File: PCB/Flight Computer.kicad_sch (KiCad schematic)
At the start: 0 parts

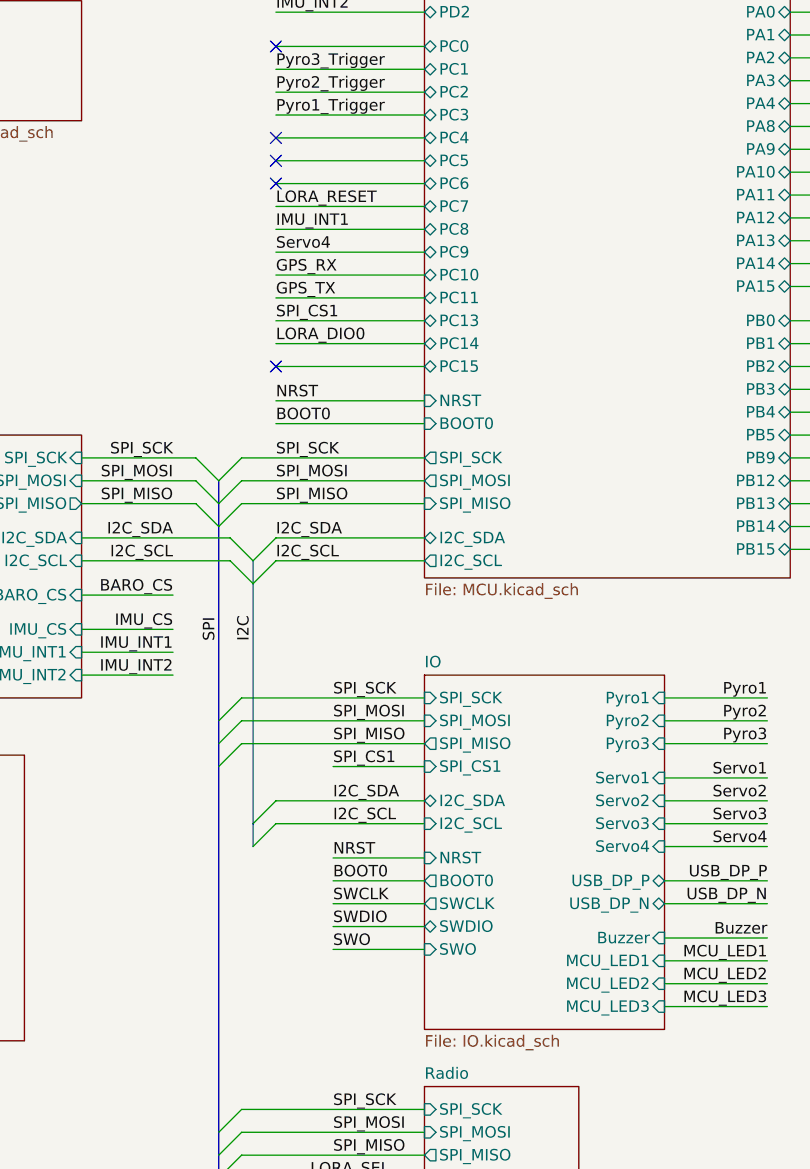
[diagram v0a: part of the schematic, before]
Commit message: Moved compass away from power traces, minor routing changes
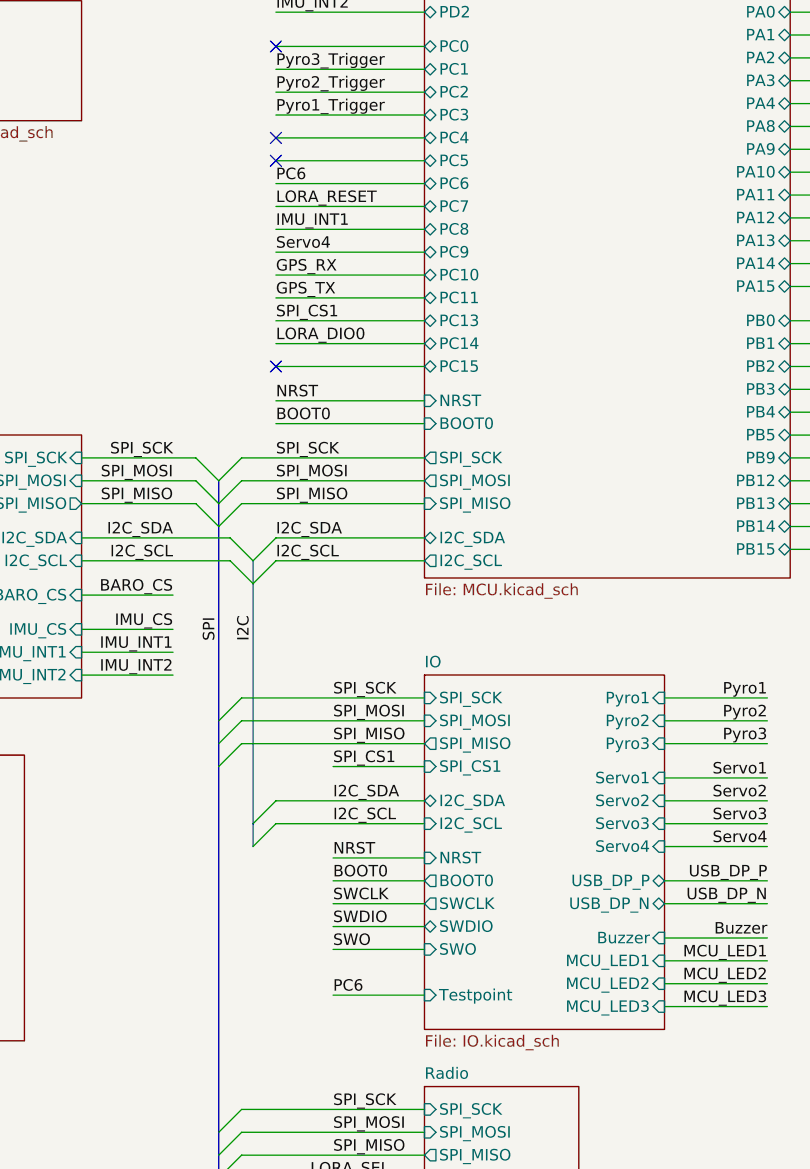
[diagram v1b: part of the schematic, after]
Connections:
- no-connect marks 15 -> 14
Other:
- sheet IO ports: added Testpoint; removed none
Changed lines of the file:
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@@
 		(at 104.14 175.26)
-	)
-	(no_connect
-		(at 100.33 50.8)
 	)
 	(bus_entry
@@
 	(wire
 		(pts
+			(xy 106.68 140.97) (xy 116.84 140.97)
+		)
+		(stroke
+			(width 0)
+			(type default)
+		)
+	)
+	(wire
+		(pts
 			(xy 157.48 81.28) (xy 173.99 81.28)
 		)
@@
 		)
 	)
+	(label "PC6"
+		(at 106.68 140.97 0)
+		(effects
+			(font
+				(size 1.27 1.27)
+			)
+			(justify left bottom)
+		)
+	)
 	(label "Pyro1_Cont"
 		(at 173.99 34.29 180)
@@
 	(label "I2C_SDA"
 		(at 106.68 119.38 0)
+		(effects
+			(font
+				(size 1.27 1.27)
+			)
+			(justify left bottom)
+		)
+	)
+	(label "PC6"
+		(at 100.33 50.8 0)
 		(effects
 			(font
@@
 			)
 		)
+		(pin "Testpoint" input
+			(at 116.84 140.97 180)
+			(effects
+				(font
+					(size 1.27 1.27)
+				)
+				(justify left)
+			)
+		)

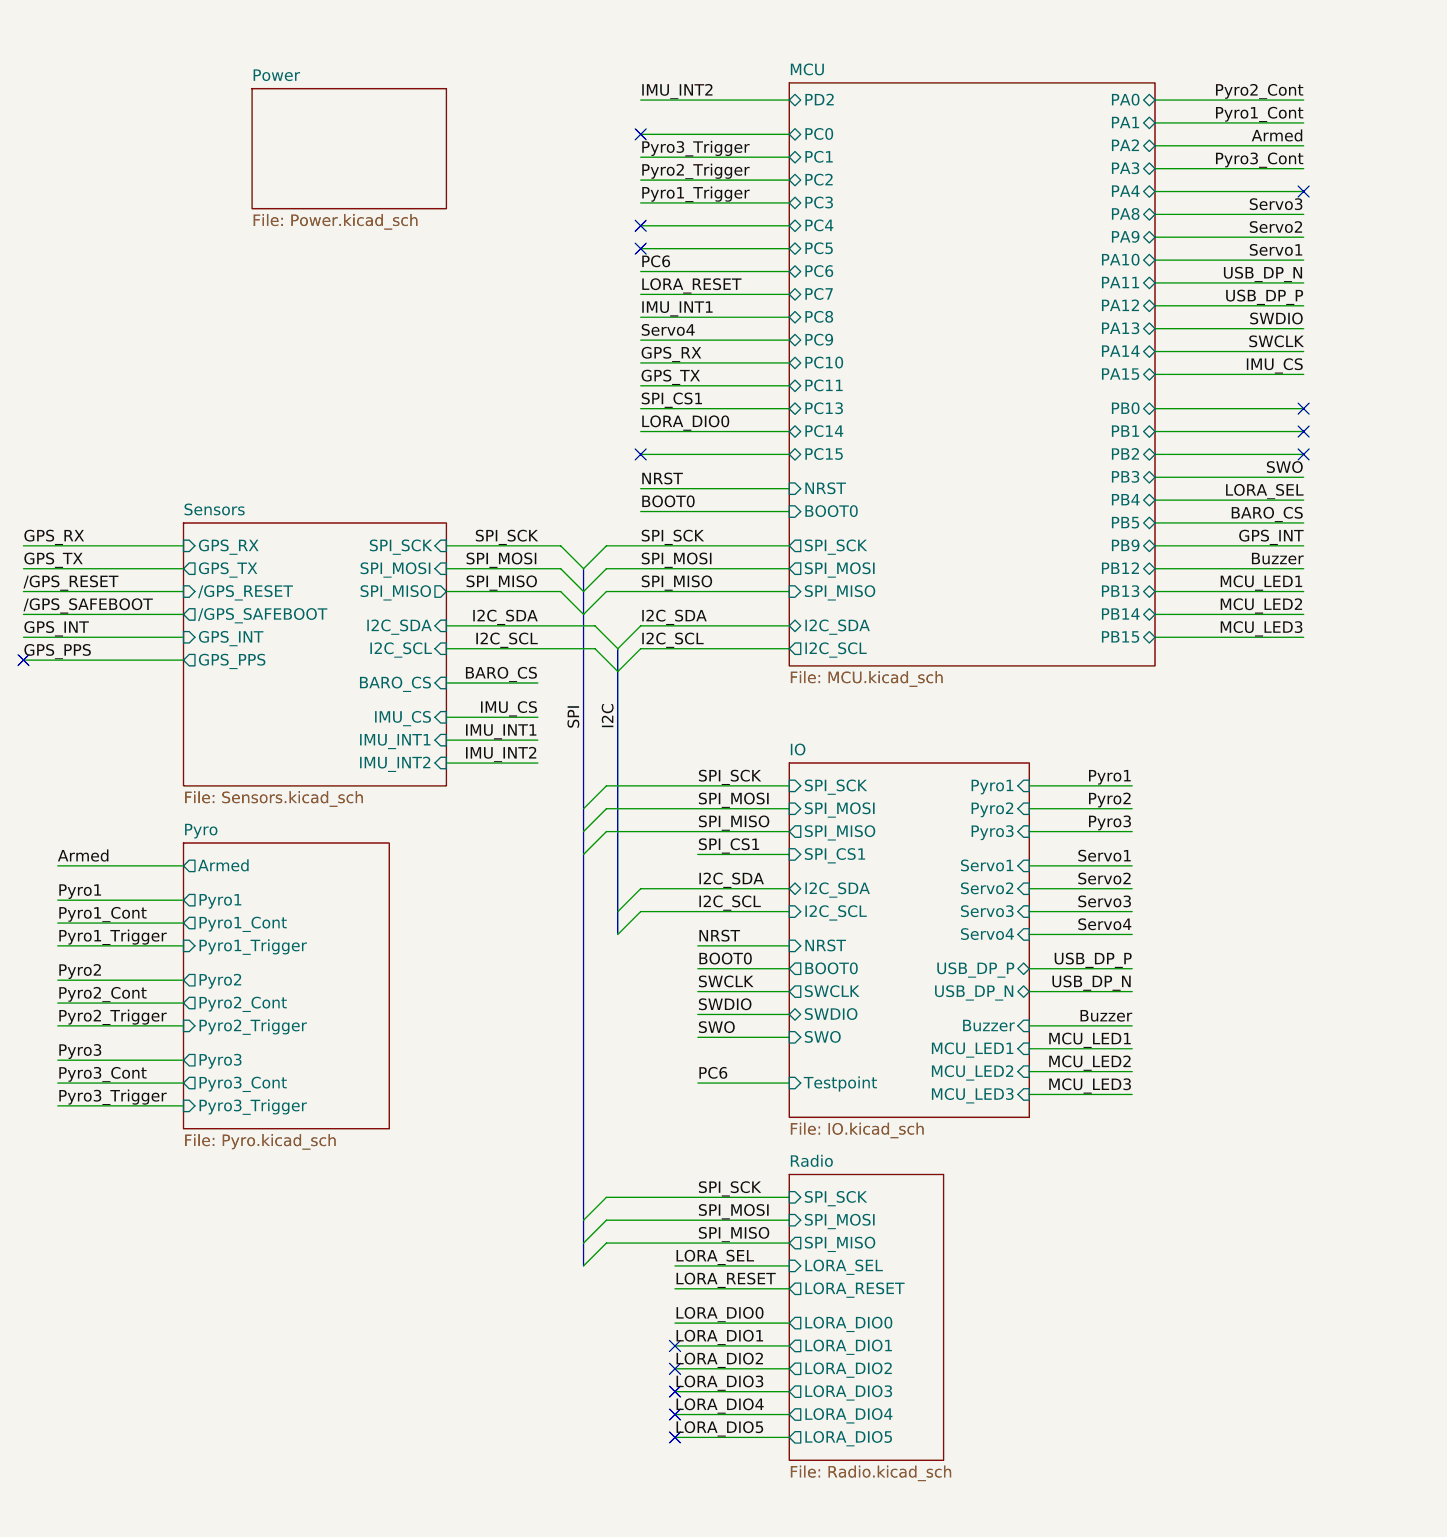
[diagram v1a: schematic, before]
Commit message: Added two more GPIO test pads
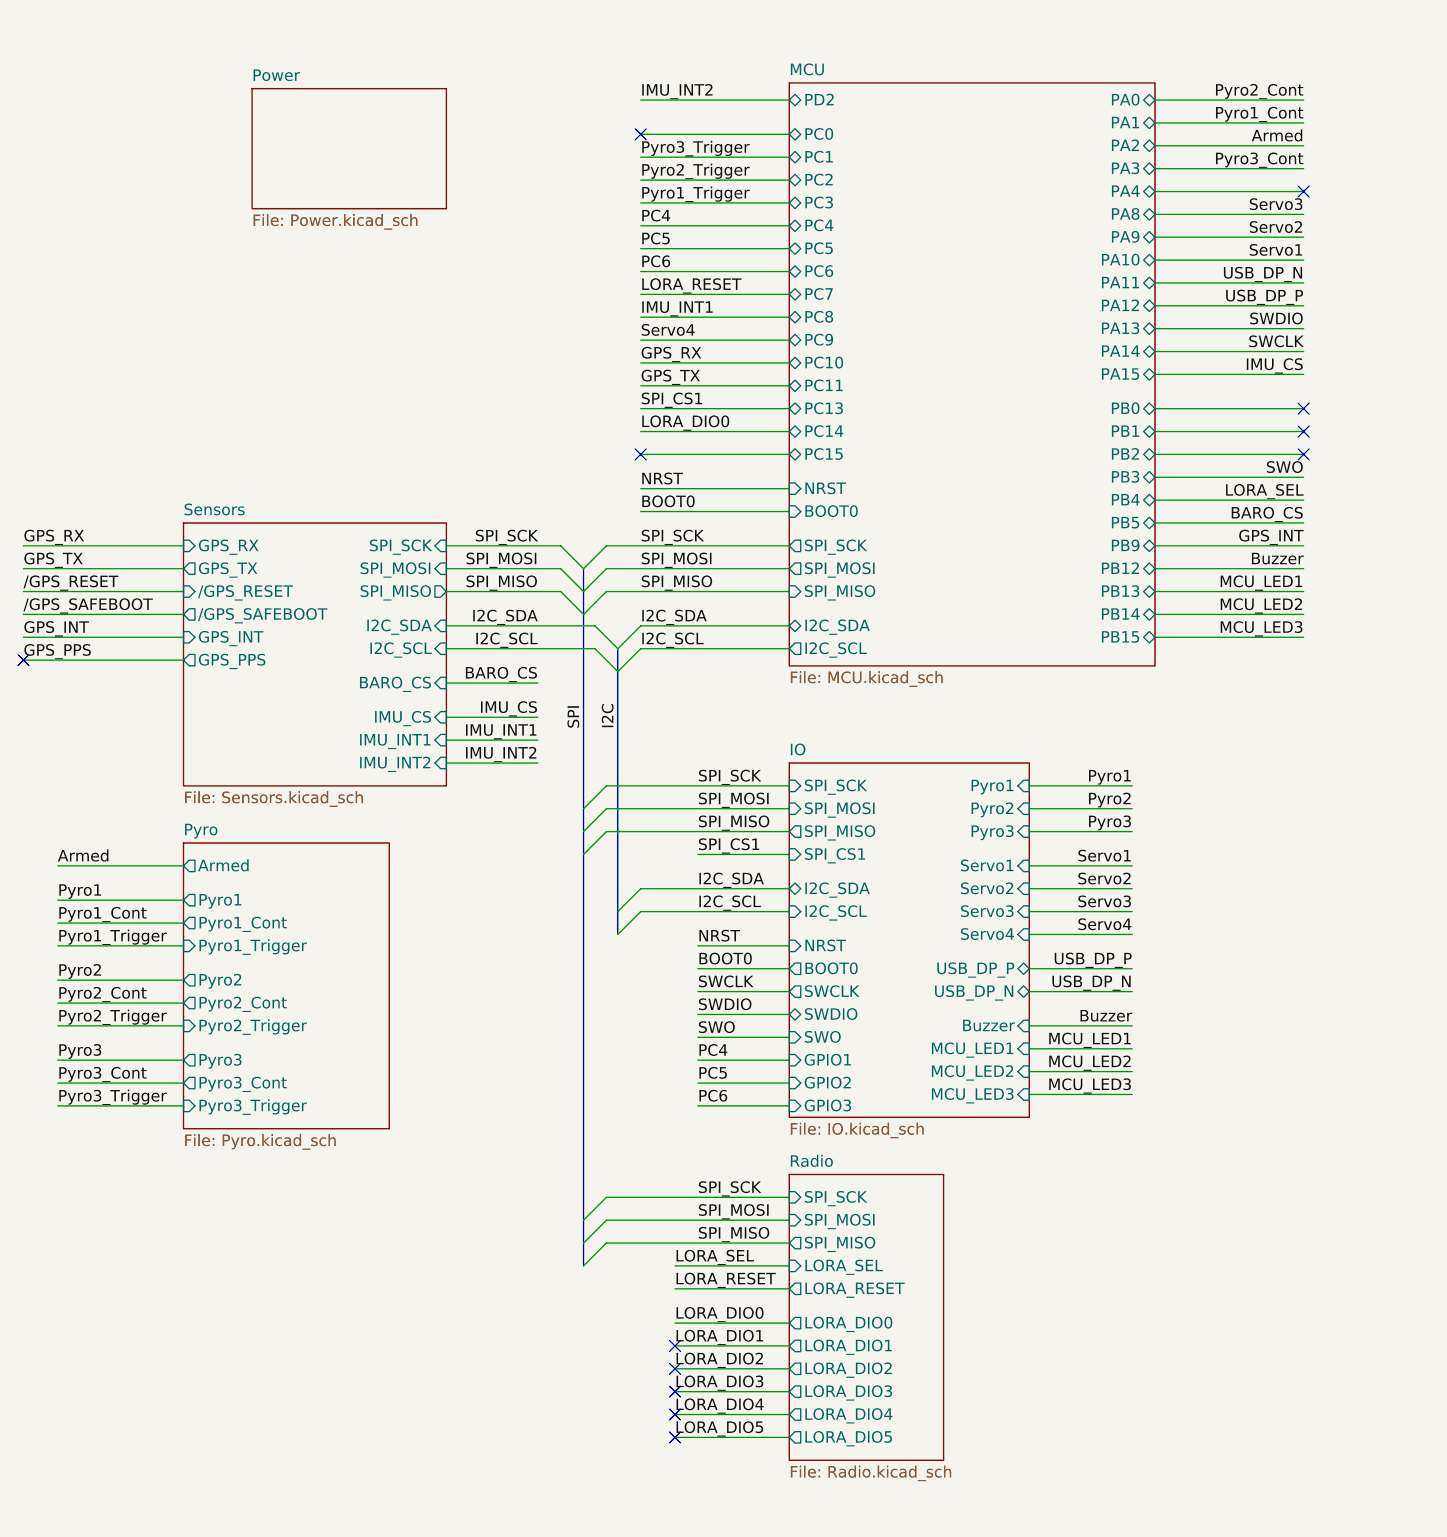
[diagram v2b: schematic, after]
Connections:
- no-connect marks 14 -> 12
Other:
- sheet IO ports: added GPIO1, GPIO2, GPIO3; removed Testpoint

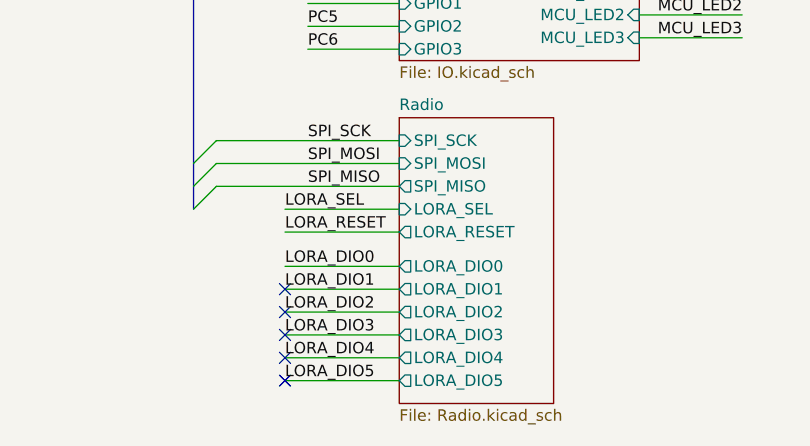
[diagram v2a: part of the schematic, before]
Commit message: Replaced the radio in the schematic
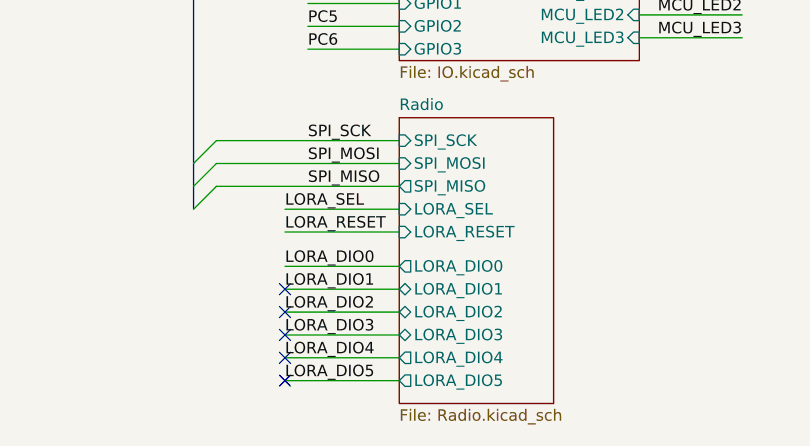
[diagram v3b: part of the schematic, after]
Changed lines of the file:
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@@
 (kicad_sch
-	(version 20250114)
+	(version 20260306)
 	(generator "eeschema")
-	(generator_version "9.0")
+	(generator_version "10.0")
 	(paper "A4")
 	(title_block
@@
 		)
 		(fill
-			(color 0 0 0 0.0000)
+			(color 0 0 0 0)
 		)
 		(property "Sheetname" "IO"
 			(at 116.84 104.6984 0)
+			(show_name no)
+			(do_not_autoplace no)
 			(effects
 				(font
@@
 		(property "Sheetfile" "IO.kicad_sch"
 			(at 116.84 145.3646 0)
+			(show_name no)
+			(do_not_autoplace no)
 			(effects
 				(font
@@
 		)
 		(fill
-			(color 0 0 0 0.0000)
+			(color 0 0 0 0)
 		)
 		(property "Sheetname" "Radio"
 			(at 116.84 150.4184 0)
+			(show_name no)
+			(do_not_autoplace no)
 			(effects
 				(font
@@
 		(property "Sheetfile" "Radio.kicad_sch"
 			(at 116.84 183.4646 0)
+			(show_name no)
+			(do_not_autoplace no)
 			(effects
 				(font
@@
 			)
 		)
-		(pin "LORA_DIO1" output
+		(pin "LORA_DIO1" bidirectional
 			(at 116.84 170.18 180)
 			(effects
@@
 			)
 		)
-		(pin "LORA_RESET" output
+		(pin "LORA_RESET" input
 			(at 116.84 163.83 180)
 			(effects
@@
 			)
 		)
-		(pin "LORA_DIO2" output
+		(pin "LORA_DIO2" bidirectional
 			(at 116.84 172.72 180)
 			(effects
@@
 			)
 		)
-		(pin "LORA_DIO3" output
+		(pin "LORA_DIO3" bidirectional
 			(at 116.84 175.26 180)
 			(effects
@@
 		)
 		(fill
-			(color 0 0 0 0.0000)
+			(color 0 0 0 0)
 		)
 		(property "Sheetname" "Sensors"
 			(at 49.53 78.0284 0)
+			(show_name no)
+			(do_not_autoplace no)
 			(effects
 				(font
@@
 		(property "Sheetfile" "Sensors.kicad_sch"
 			(at 49.53 108.5346 0)
+			(show_name no)
+			(do_not_autoplace no)
 			(effects
 				(font
@@
 		)
 		(fill
-			(color 0 0 0 0.0000)
+			(color 0 0 0 0)
 		)
 		(property "Sheetname" "Power"
 			(at 57.15 29.7684 0)
+			(show_name no)
+			(do_not_autoplace no)
 			(effects
 				(font
@@
 		(property "Sheetfile" "Power.kicad_sch"
 			(at 57.15 44.3996 0)
+			(show_name no)
+			(do_not_autoplace no)
 			(effects
 				(font
@@
 		)
 		(fill
-			(color 0 0 0 0.0000)
+			(color 0 0 0 0)
 		)
 		(property "Sheetname" "MCU"
 			(at 116.84 29.1334 0)
+			(show_name no)
+			(do_not_autoplace no)
 			(effects
 				(font
@@
 		(property "Sheetfile" "MCU.kicad_sch"
 			(at 116.84 95.1996 0)
+			(show_name no)
+			(do_not_autoplace no)
 			(effects
 				(font
@@
 		)
 		(fill
-			(color 0 0 0 0.0000)
+			(color 0 0 0 0)
 		)
 		(property "Sheetname" "Pyro"
 			(at 49.53 113.5884 0)
+			(show_name no)
+			(do_not_autoplace no)
 			(effects
 				(font
@@
 		(property "Sheetfile" "Pyro.kicad_sch"
 			(at 49.53 146.6346 0)
+			(show_name no)
+			(do_not_autoplace no)
 			(effects
 				(font
